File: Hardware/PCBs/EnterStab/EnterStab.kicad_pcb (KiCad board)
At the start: 2 copper layers, 62 x 9 mm, 4 parts

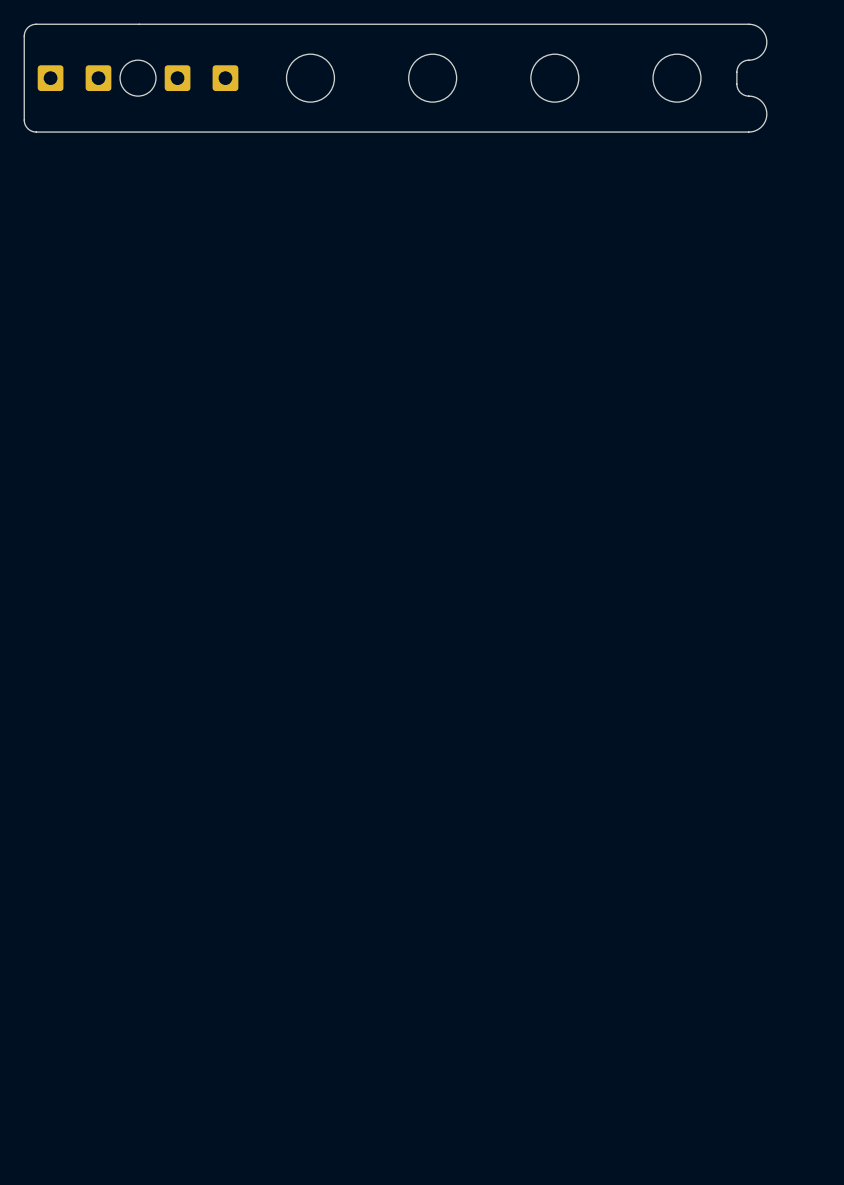
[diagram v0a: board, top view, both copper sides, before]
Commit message: Update enter stab; add new renders
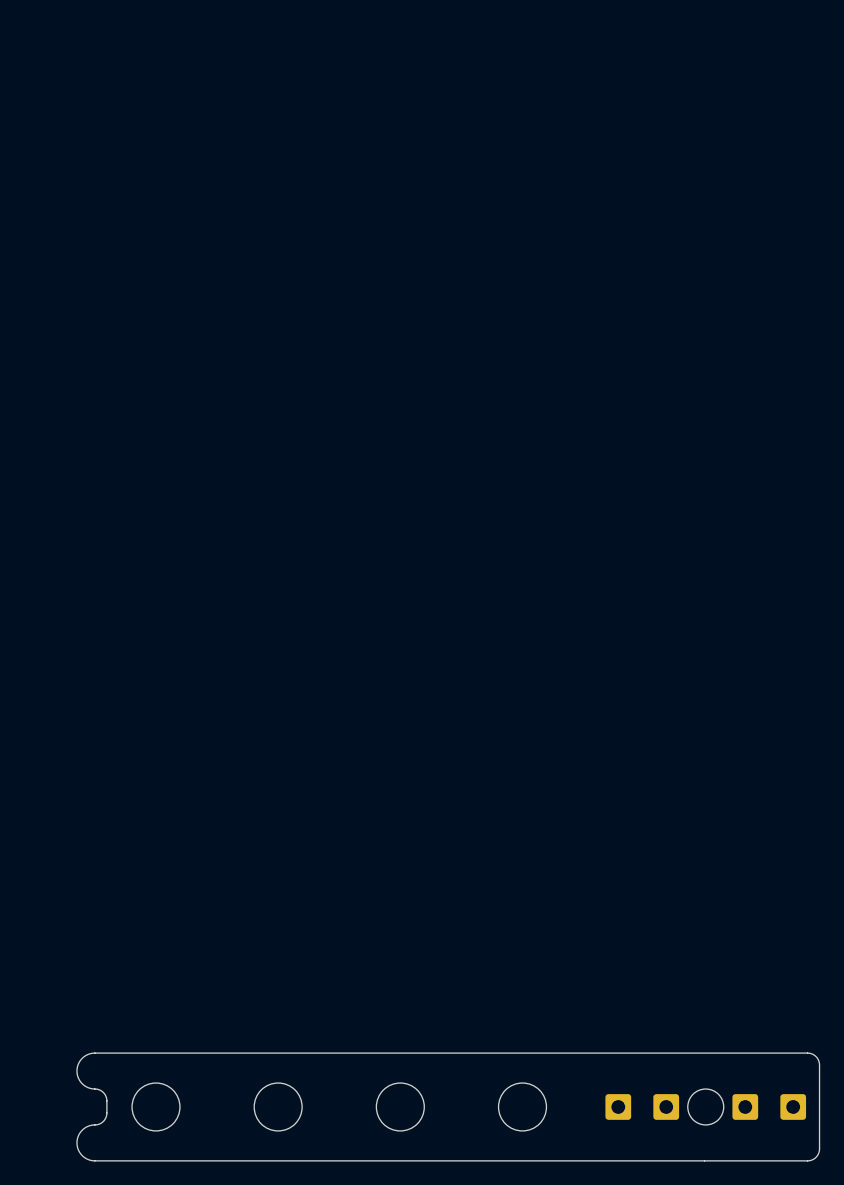
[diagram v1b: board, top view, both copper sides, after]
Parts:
- moved P4a 105.9 mm to (104.2, 130.4), turned to 90 degrees
- moved P2a 101.5 mm to (100.2, 130.4), turned to 90 degrees
- moved P3a 95.1 mm to (93.6, 130.4), turned to 90 degrees
- moved P5a 91.9 mm to (89.6, 130.4), turned to 90 degrees
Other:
- outline, holes or cut-outs redrawn
- board text added: "PCB3D_BR_ENTERSTAB"
- board text added: "PCB3D_TL_ENTERSTAB"
